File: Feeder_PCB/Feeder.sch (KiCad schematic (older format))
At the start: 1 part

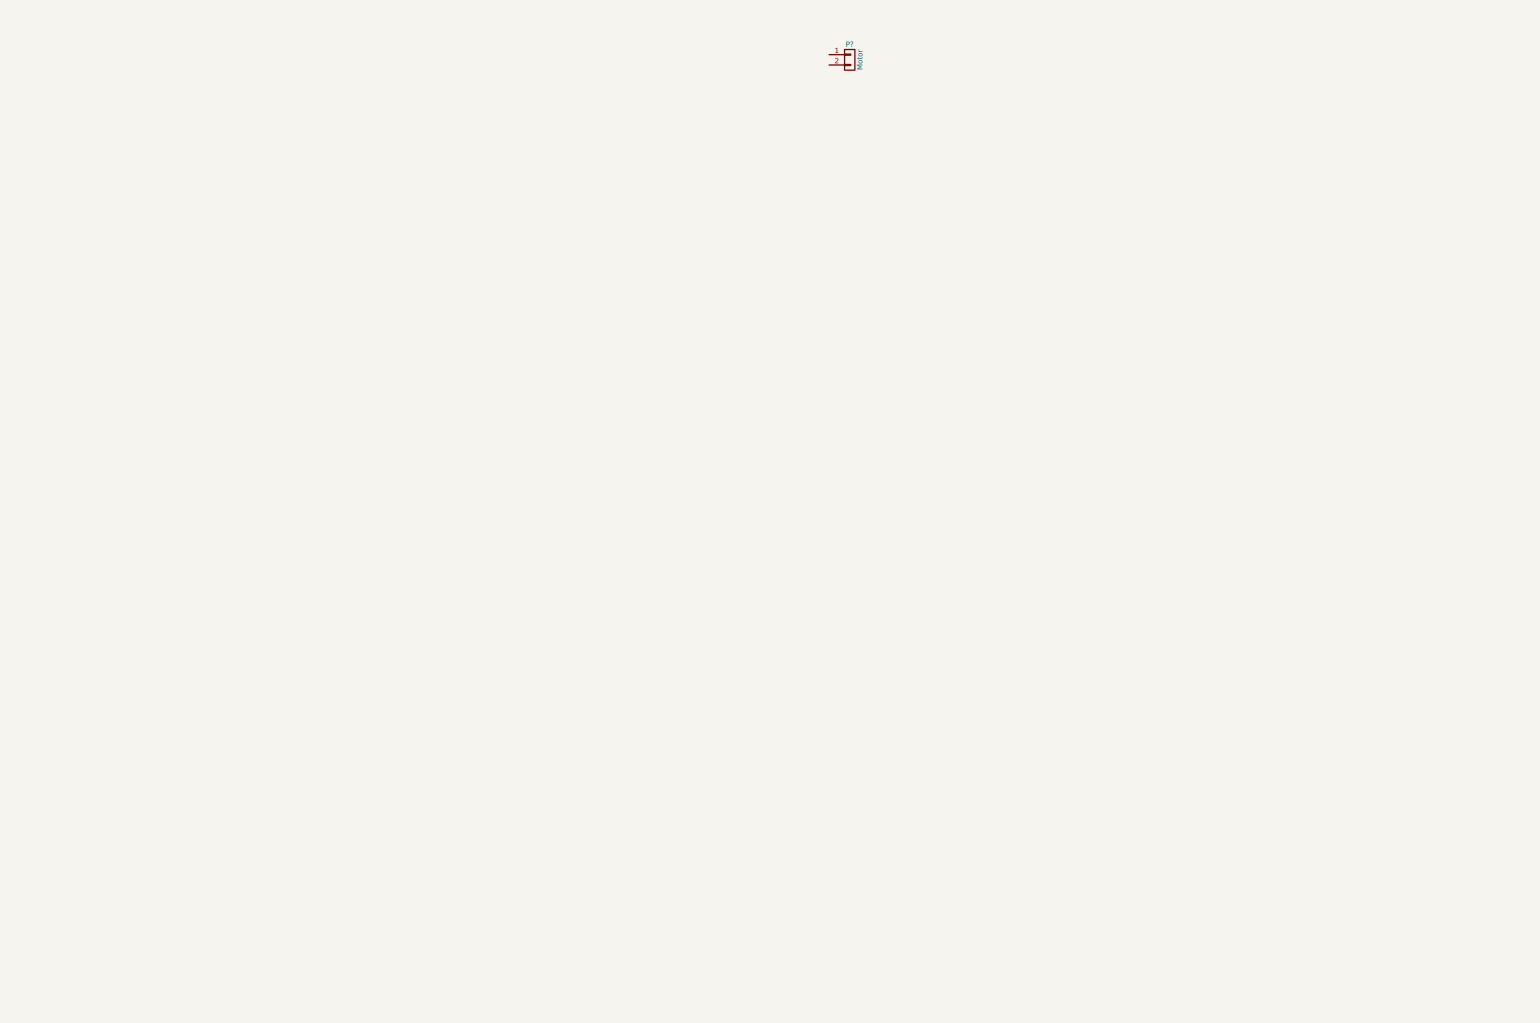
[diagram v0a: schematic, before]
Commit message: Schaltplan und Netzliste für Testboard erstellt
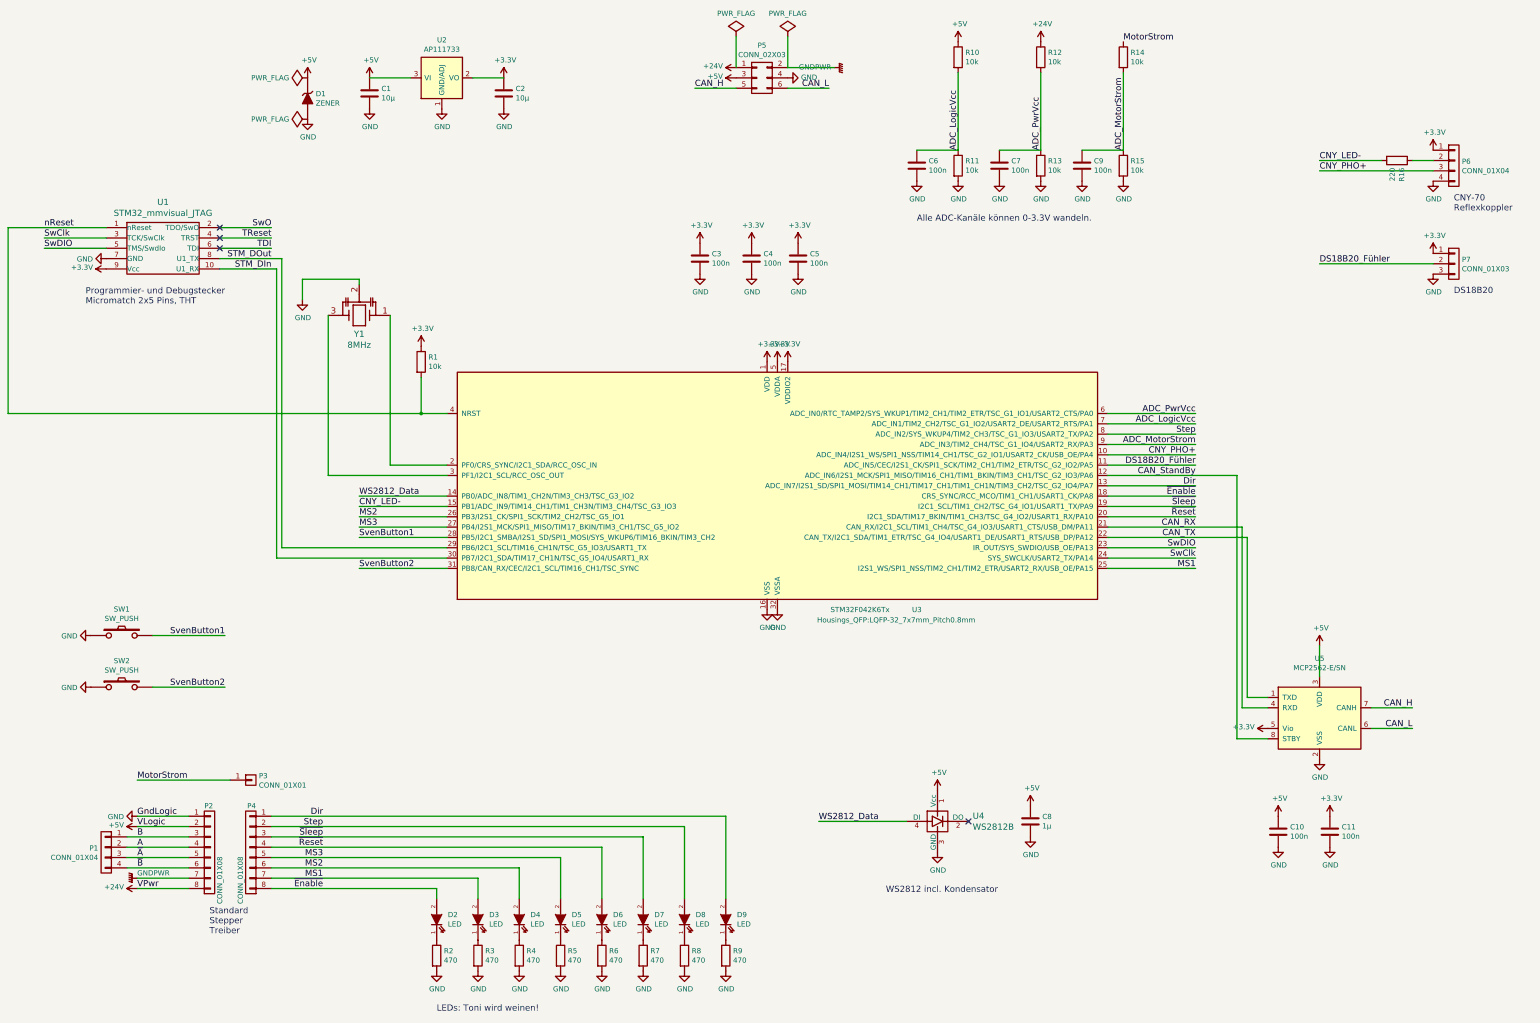
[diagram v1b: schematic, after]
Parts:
- removed P?: Motor, symbol CONN_01X02
- added C1, C2: 10µ, Capacitors_SMD:C_0805, symbol C
- added C10, C11, C3, C4, C5, C6, C7, C9: 100n, Capacitors_SMD:C_0603, symbol C
- added C8: 1µ, Capacitors_SMD:C_0603, symbol C
- added D1: ZENER, Diodes_SMD:D_MiniMELF_Standard, symbol ZENER
- added D2, D3, D4, D5, D6, D7, D8, D9: LED, LEDs:LED_0603, symbol LED
- added P1: CONN_01X04, Connectors_JST:JST_XH_B04B-XH-A_04x2.50mm_Straight, symbol CONN_01X04
- added P2, P4: CONN_01X08, Socket_Strips:Socket_Strip_Straight_1x08_Pitch2.54mm, symbol CONN_01X08
- added P3: CONN_01X01, Pin_Headers:Pin_Header_Angled_1x01_Pitch2.54mm, symbol CONN_01X01
- added P5: CONN_02X03, Pin_Headers:Pin_Header_Angled_2x03_Pitch2.54mm, symbol CONN_02X03
- added P6: CONN_01X04, Connectors_JST:JST_PH_B4B-PH-K_04x2.00mm_Straight, symbol CONN_01X04
- added P7: CONN_01X03, Pin_Headers:Pin_Header_Angled_1x03_Pitch2.54mm, symbol CONN_01X03
- added R1, R10, R11, R12, R13, R14, R15: 10k, Resistors_SMD:R_0603, symbol R
- added R16: 220, Resistors_SMD:R_0603, symbol R
- added R2, R3, R4, R5, R6, R7, R8, R9: 470, Resistors_SMD:R_0603, symbol R
- added SW1, SW2: SW_PUSH, symbol SW_PUSH
- added U1: STM32_mmvisual_JTAG, PhilippsFootprints:MICROMATCH-10, symbol STM32_mmvisual_JTAG
- added U2: AP111733, TO_SOT_Packages_SMD:SOT-223, symbol AP111733
- added U3: STM32F042K6Tx, Housings_QFP:LQFP-32_7x7mm_Pitch0.8mm, symbol STM32F042K6Tx
- added U4: WS2812B, LEDs:LED_WS2812B-PLCC4, symbol WS2812B
- added U5: MCP2562-E/SN, Housings_SOIC:SOIC-8_3.9x4.9mm_Pitch1.27mm, symbol MCP2562-E/SN
- added Y1: 8MHz, PhilippsFootprints:CSTCE_3,2x1,3, symbol RESONATEUR
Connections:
- new net: U3.2 (PF0/CRS_SYNC/I2C1_SDA/RCC_OSC_IN), Y1.1
- new net: U3.3 (PF1/I2C1_SCL/RCC_OSC_OUT), Y1.3
- new net: D2.1 (K), R2.1
- new net: D3.1 (K), R3.1
- new net: D4.1 (K), R4.1
- new net: D5.1 (K), R5.1
- new net: D6.1 (K), R6.1
- new net: D7.1 (K), R7.1
- new net: D8.1 (K), R8.1
- new net: D9.1 (K), R9.1
- new net: P6.2 (P2), R16.1
- new net +24V: P2.8 (P8), P5.1 (P1), R12.1
- new net +3V3: C11.1, C2.1, C3.1, C4.1, C5.1, P6.1 (P1), P7.1 (P1), R1.1, U1.9 (Vcc), U2.2 (VO), U2.4 (VO), U3.1 (VDD), U3.17 (VDDIO2), U3.5 (VDDA), U5.5 (Vio)
- new net +5V: C1.1, C10.1, C8.1, D1.1 (K), P2.2 (P2), P5.3 (P3), R10.1, U2.3 (VI), U4.1 (Vcc), U5.3 (VDD)
- new net A: P1.2 (P2), P2.4 (P4)
- new net ADC_LogicVcc: C6.1, R10.2, R11.1, U3.7 (ADC_IN1/TIM2_CH2/TSC_G1_IO2/USART2_DE/USART2_RTS/PA1)
- new net ADC_MotorStrom: C9.1, R14.2, R15.1, U3.9 (ADC_IN3/TIM2_CH4/TSC_G1_IO4/USART2_RX/PA3)
- new net ADC_PwrVcc: C7.1, R12.2, R13.1, U3.6 (ADC_IN0/RTC_TAMP2/SYS_WKUP1/TIM2_CH1/TIM2_ETR/TSC_G1_IO1/USART2_CTS/PA0)
- new net B: P1.1 (P1), P2.3 (P3)
- new net CAN_H: P5.5 (P5), U5.7 (CANH)
- new net CAN_L: P5.6 (P6), U5.6 (CANL)
- new net CAN_RX: U3.21 (CAN_RX/I2C1_SCL/TIM1_CH4/TSC_G4_IO3/USART1_CTS/USB_DM/PA11), U5.4 (RXD)
- new net CAN_StandBy: U3.12 (ADC_IN6/I2S1_MCK/SPI1_MISO/TIM16_CH1/TIM1_BKIN/TIM3_CH1/TSC_G2_IO3/PA6), U5.8 (STBY)
- new net CAN_TX: U3.22 (CAN_TX/I2C1_SDA/TIM1_ETR/TSC_G4_IO4/USART1_DE/USART1_RTS/USB_DP/PA12), U5.1 (TXD)
- new net CNY_LED-: R16.2, U3.15 (PB1/ADC_IN9/TIM14_CH1/TIM1_CH3N/TIM3_CH4/TSC_G3_IO3)
- new net CNY_PHO+: P6.3 (P3), U3.10 (ADC_IN4/I2S1_WS/SPI1_NSS/TIM14_CH1/TSC_G2_IO1/USART2_CK/USB_OE/PA4)
- new net DS18B20_Fühler: P7.2 (P2), U3.11 (ADC_IN5/CEC/I2S1_CK/SPI1_SCK/TIM2_CH1/TIM2_ETR/TSC_G2_IO2/PA5)
- new net Dir: D9.2 (A), P4.1 (P1), U3.13 (ADC_IN7/I2S1_SD/SPI1_MOSI/TIM14_CH1/TIM17_CH1/TIM1_CH1N/TIM3_CH2/TSC_G2_IO4/PA7)
- new net GND: C1.2, C10.2, C11.2, C2.2, C3.2, C4.2, C5.2, C6.2, C7.2, C8.2, C9.2, D1.2 (A), P2.1 (P1), P5.4 (P4), P6.4 (P4), P7.3 (P3), R11.2, R13.2, R15.2, R2.2, R3.2, R4.2, R5.2, R6.2, R7.2, R8.2, R9.2, SW1.1, SW2.1, U1.7 (GND), U2.1 (GND/ADJ), U3.16 (VSS), U3.32 (VSSA), U4.3 (GND), U5.2 (VSS), Y1.2
- new net GNDPWR: P2.7 (P7), P5.2 (P2)
- new net MS1: D3.2 (A), P4.7 (P7), U3.25 (I2S1_WS/SPI1_NSS/TIM2_CH1/TIM2_ETR/USART2_RX/USB_OE/PA15)
- new net MS2: D4.2 (A), P4.6 (P6), U3.26 (PB3/I2S1_CK/SPI1_SCK/TIM2_CH2/TSC_G5_IO1)
- new net MS3: D5.2 (A), P4.5 (P5), U3.27 (PB4/I2S1_MCK/SPI1_MISO/TIM17_BKIN/TIM3_CH1/TSC_G5_IO2)
- new net MotorStrom: P3.1 (P1), R14.1
- new net STM_DIn: U1.10 (U1_RX), U3.30 (PB7/I2C1_SDA/TIM17_CH1N/TSC_G5_IO4/USART1_RX)
- new net STM_DOut: U1.8 (U1_TX), U3.29 (PB6/I2C1_SCL/TIM16_CH1N/TSC_G5_IO3/USART1_TX)
- new net Step: D8.2 (A), P4.2 (P2), U3.8 (ADC_IN2/SYS_WKUP4/TIM2_CH3/TSC_G1_IO3/USART2_TX/PA2)
- new net SvenButton1: SW1.2, U3.28 (PB5/I2C1_SMBA/I2S1_SD/SPI1_MOSI/SYS_WKUP6/TIM16_BKIN/TIM3_CH2)
- new net SvenButton2: SW2.2, U3.31 (PB8/CAN_RX/CEC/I2C1_SCL/TIM16_CH1/TSC_SYNC)
- new net SwClk: U1.3 (TCK/SwClk), U3.24 (SYS_SWCLK/USART2_TX/PA14)
- new net SwDIO: U1.5 (TMS/SwdIo), U3.23 (IR_OUT/SYS_SWDIO/USB_OE/PA13)
- new net SwO: U1.2 (TDO/SwO)
- new net TDI: U1.6 (TDI)
- new net TReset: U1.4 (TRST)
- new net WS2812_Data: U3.14 (PB0/ADC_IN8/TIM1_CH2N/TIM3_CH3/TSC_G3_IO2), U4.4 (DI)
- new net nReset: R1.2, U1.1 (nReset), U3.4 (NRST)
- new net ~A: P1.3 (P3), P2.5 (P5)
- new net ~B: P1.4 (P4), P2.6 (P6)
- new net ~Enable: D2.2 (A), P4.8 (P8), U3.18 (CRS_SYNC/RCC_MCO/TIM1_CH1/USART1_CK/PA8)
- new net ~Reset: D6.2 (A), P4.4 (P4), U3.20 (I2C1_SDA/TIM17_BKIN/TIM1_CH3/TSC_G4_IO2/USART1_RX/PA10)
- new net ~Sleep: D7.2 (A), P4.3 (P3), U3.19 (I2C1_SCL/TIM1_CH2/TSC_G4_IO1/USART1_TX/PA9)
- no-connect marks 0 -> 4
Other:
- note added: "Alle ADC-Kanäle können 0-3.3V wandeln."
- note added: "CNY-70\nReflexkoppler"
- note added: "DS18B20"
- note added: "LEDs: Toni wird weinen!"
- note added: "Programmier- und Debugstecker\nMicromatch 2x5 Pins, THT"
- note added: "Standard\nStepper\nTreiber"
- note added: "WS2812 incl. Kondensator"
